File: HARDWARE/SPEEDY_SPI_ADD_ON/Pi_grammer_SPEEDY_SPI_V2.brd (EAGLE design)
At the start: 22.9 x 61 mm, 11 parts, among them J2 TARGET_copy

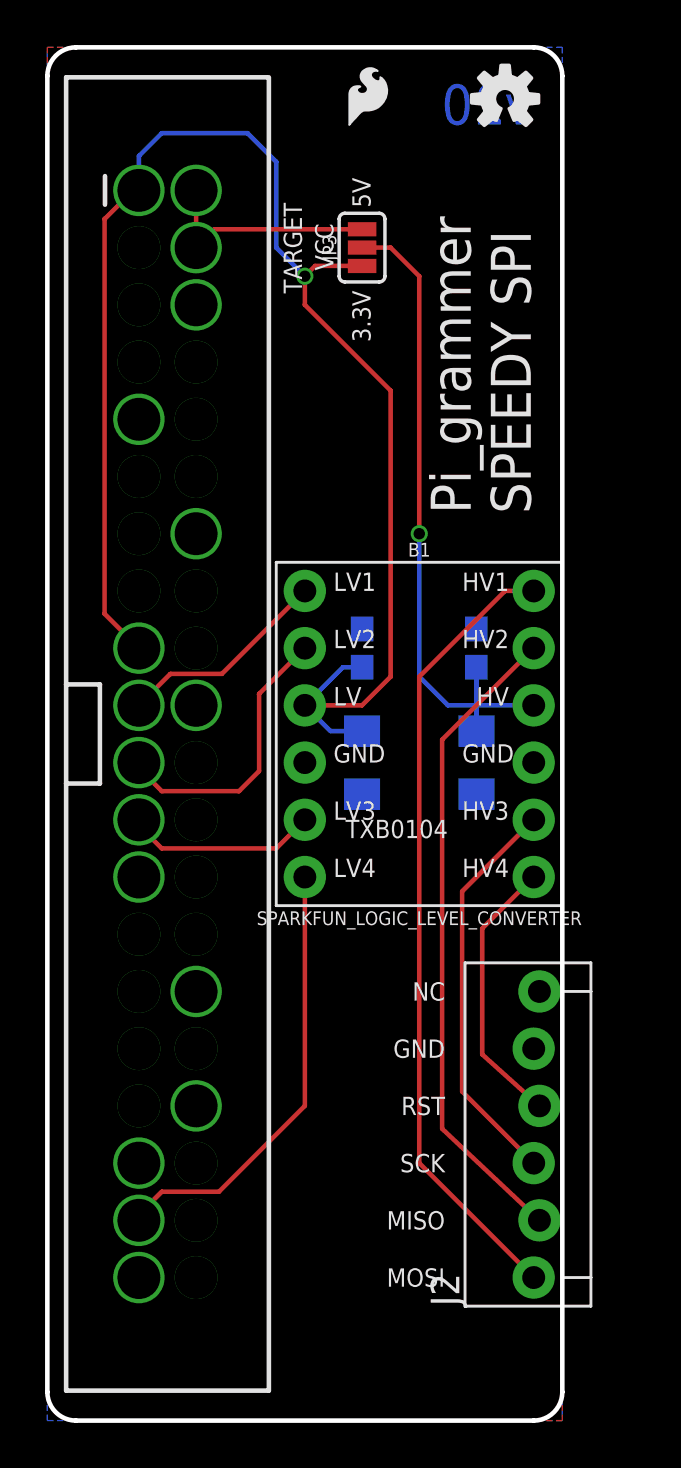
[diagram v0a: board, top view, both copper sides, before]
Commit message: SPEED SPI layout work
locking footprint on converter.

moved to 16 mils traces everywhere.

curved traces to keep length of data lines as similar as possible.

removed pin 20 GND on PI header. Not necessary and wanted more clearance
from nearby data trace.
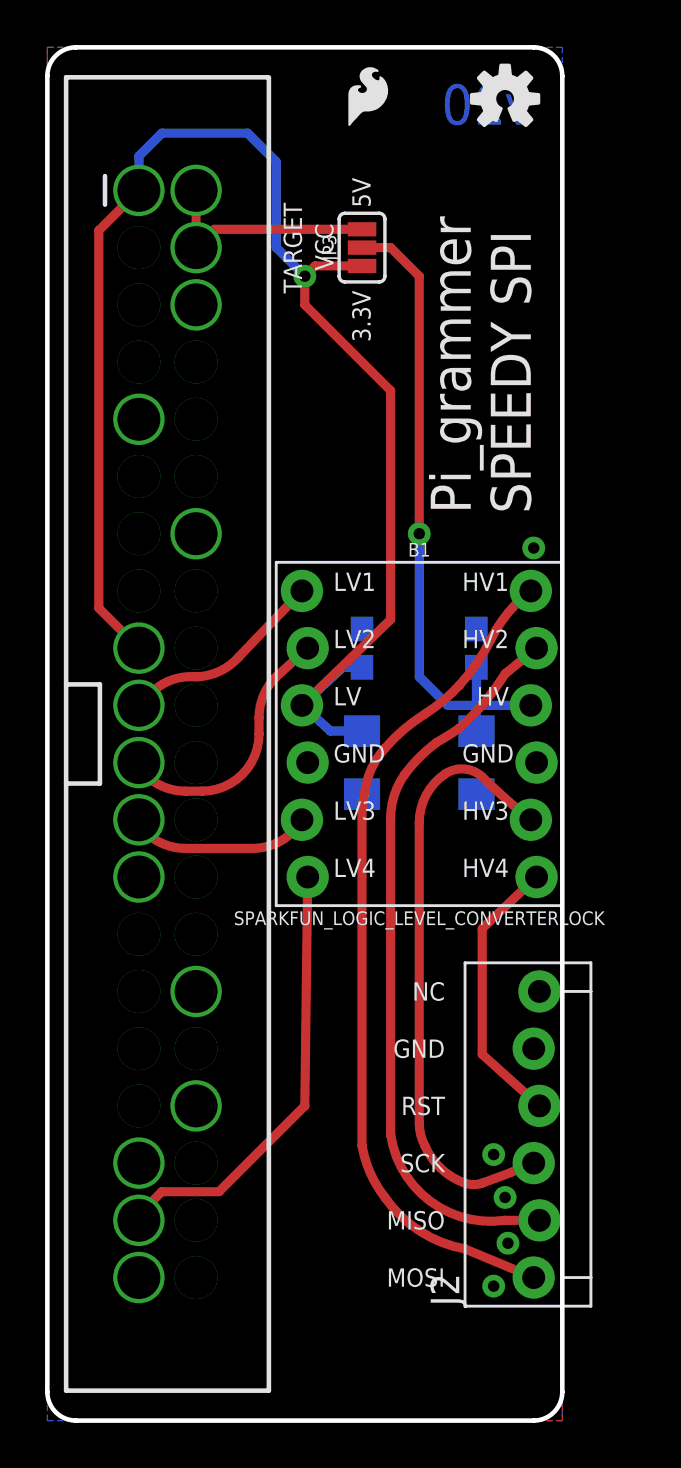
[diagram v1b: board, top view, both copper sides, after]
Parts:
- B1: value SPARKFUN_LOGIC_LEVEL_CONVERTER -> SPARKFUN_LOGIC_LEVEL_CONVERTERLOCK; device SparkFun-Boards:SPARKFUN_LOGIC_LEVEL_CONVERTER -> SparkFun-Boards:SPARKFUN_LOGIC_LEVEL_CONVERTER_LOCK
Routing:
- net SCK_T: track 17.9 -> 27.0 mm
- net MISO_T: track 28.9 -> 32.1 mm
- net MOSI_T: track 35.4 -> 37.5 mm
- net MISO: track 12.7 -> 11.5 mm
- net 3.3V: track 68.6 -> 67.4 mm
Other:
- board text removed: "TXB0104"
